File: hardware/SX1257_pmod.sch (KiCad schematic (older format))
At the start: 50 parts, among them J1 Conn_02x06_Odd_Even, J2 SMA_F_RX, J3 SMA_F_TX, U1 SX1257, U2 SC18IS602B, Y1 32/36MHz ?ppm

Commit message: PCB design almost done.
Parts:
- removed AE1, AE2: PCB_Ant, symbol Device:Antenna
- removed R3, R4, R5, R6: 0R, Resistor_SMD:R_0603_1608Metric, symbol Device:R
- J2, J3: footprint Connector_Coaxial:SMA_Amphenol_132134-10_Vertical -> extra:CON-SMA-EDGE
- Y1: value 32/36MHz ?ppm -> 36MHz 10ppm; footprint Crystal:Crystal_SMD_5032-4Pin_5.0x3.2mm -> Crystal:Crystal_SMD_3225-4Pin_3.2x2.5mm; MfrNo (none) -> ABM8-36.000MHZ-10-1-U-T; Mouser (none) -> 815-ABM8-36-10-1-U-T; MouserURL (none) -> https://www.mouser.se/ProductDetail/ABRACON/ABM8-36000MHZ-1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
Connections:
- wire segments 186 -> 176
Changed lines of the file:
@@
 P 7450 4500
 F 0 "Y1" H 7500 4700 50  0000 L CNN
-F 1 "32/36MHz ?ppm" H 7500 4800 50  0000 L CNN
-F 2 "Crystal:Crystal_SMD_5032-4Pin_5.0x3.2mm" H 7450 4500 50  0001 C CNN
-F 3 "~" H 7450 4500 50  0001 C CNN
+F 1 "36MHz 10ppm" H 7500 4800 50  0000 L CNN
+F 2 "Crystal:Crystal_SMD_3225-4Pin_3.2x2.5mm" H 7450 4500 50  0001 C CNN
+F 3 "https://www.mouser.se/datasheet/2/3/abm8-16794.pdf" H 7450 4500 50  0001 C CNN
+F 4 "815-ABM8-36-10-1-U-T" H 7450 4500 50  0001 C CNN "Mouser"
+F 5 "https://www.mouser.se/ProductDetail/ABRACON/ABM8-36000MHZ-10-1-U-T?qs=sGAEpiMZZMsBj6bBr9Q9acVJ3l36SOAPXI0xqgGUahk%3d" H 7450 4500 50  0001 C CNN "MouserURL"
+F 6 "ABM8-36.000MHZ-10-1-U-T" H 7450 4500 50  0001 C CNN "MfrNo"
 	1    7450 4500
 	1    0    0    -1
@@
 F 0 "J3" H 4499 5276 50  0000 L CNN
 F 1 "SMA_F_TX" H 4499 5185 50  0000 L CNN
-F 2 "Connector_Coaxial:SMA_Amphenol_132134-10_Vertical" H 4400 5300 50  0001 C CNN
+F 2 "extra:CON-SMA-EDGE" H 4400 5300 50  0001 C CNN
 F 3 " ~" H 4400 5300 50  0001 C CNN
 	1    4400 5300
@@
 Wire Wire Line
 	1450 6200 1450 6100
-Wire Wire Line
-	3450 5300 3550 5300
 $Comp
 L Device:C C5
@@
 Registers are available\nthrough SPI.
 $Comp
-L Device:Antenna AE2
-U 1 1 5C4B8B38
-P 4400 5100
-F 0 "AE2" V 4354 5230 50  0000 L CNN
-F 1 "PCB_Ant" V 4445 5230 50  0000 L CNN
-F 2 "" H 4400 5100 50  0001 C CNN
-F 3 "~" H 4400 5100 50  0001 C CNN
-	1    4400 5100
-	0    1    1    0
-$EndComp
-$Comp
-L Device:R R6
-U 1 1 5C4C50F2
-P 3850 5300
-F 0 "R6" V 3900 5450 50  0000 C CNN
-F 1 "0R" V 3850 5300 50  0000 C CNN
-F 2 "Resistor_SMD:R_0603_1608Metric" V 3780 5300 50  0001 C CNN
-F 3 "~" H 3850 5300 50  0001 C CNN
-	1    3850 5300
-	0    1    1    0
-$EndComp
-$Comp
-L Device:R R5
-U 1 1 5C4D0A85
-P 3850 5100
-F 0 "R5" V 3900 5250 50  0000 C CNN
-F 1 "0R" V 3850 5100 50  0000 C CNN
-F 2 "Resistor_SMD:R_0603_1608Metric" V 3780 5100 50  0001 C CNN
-F 3 "~" H 3850 5100 50  0001 C CNN
-	1    3850 5100
-	0    1    1    0
-$EndComp
-Wire Wire Line
-	3700 5100 3550 5100
-Wire Wire Line
-	3550 5100 3550 5300
-Connection ~ 3550 5300
-Wire Wire Line
-	3550 5300 3700 5300
-Wire Wire Line
-	4000 5100 4200 5100
-Wire Wire Line
-	4000 5300 4200 5300
-$Comp
 L Connector:Conn_Coaxial J2
 U 1 1 5C4EEF69
@@
 F 0 "J2" H 4499 3926 50  0000 L CNN
 F 1 "SMA_F_RX" H 4499 3835 50  0000 L CNN
-F 2 "Connector_Coaxial:SMA_Amphenol_132134-10_Vertical" H 4400 3950 50  0001 C CNN
+F 2 "extra:CON-SMA-EDGE" H 4400 3950 50  0001 C CNN
 F 3 " ~" H 4400 3950 50  0001 C CNN
 	1    4400 3950
@@
 Wire Wire Line
 	4400 4450 4400 4150
-$Comp
-L Device:Antenna AE1
-U 1 1 5C4EEF78
-P 4400 3750
-F 0 "AE1" V 4354 3880 50  0000 L CNN
-F 1 "PCB_Ant" V 4445 3880 50  0000 L CNN
-F 2 "" H 4400 3750 50  0001 C CNN
-F 3 "~" H 4400 3750 50  0001 C CNN
-	1    4400 3750
-	0    1    1    0
-$EndComp
-$Comp
-L Device:R R4
-U 1 1 5C4EEF7F
-P 3850 3950
-F 0 "R4" V 3900 4100 50  0000 C CNN
-F 1 "0R" V 3850 3950 50  0000 C CNN
-F 2 "Resistor_SMD:R_0603_1608Metric" V 3780 3950 50  0001 C CNN
-F 3 "~" H 3850 3950 50  0001 C CNN
-	1    3850 3950
-	0    1    1    0
-$EndComp
-$Comp
-L Device:R R3
-U 1 1 5C4EEF86
-P 3850 3750
-F 0 "R3" V 3900 3900 50  0000 C CNN
-F 1 "0R" V 3850 3750 50  0000 C CNN
-F 2 "Resistor_SMD:R_0603_1608Metric" V 3780 3750 50  0001 C CNN
-F 3 "~" H 3850 3750 50  0001 C CNN
-	1    3850 3750
-	0    1    1    0
-$EndComp
-Wire Wire Line
-	3700 3750 3550 3750
-Wire Wire Line
-	3550 3750 3550 3950
-Wire Wire Line
-	3550 3950 3700 3950
-Wire Wire Line
-	4000 3750 4200 3750
-Wire Wire Line
-	4000 3950 4200 3950
-Wire Wire Line
-	3550 3950 3250 3950
-Connection ~ 3550 3950
 Connection ~ 3250 3950
 Text Label 1000 1150 2    50   ~ 0
@@
 Wire Wire Line
 	13050 1500 13250 1500
+Wire Wire Line
+	3250 3950 4200 3950
+Wire Wire Line
+	3450 5300 4200 5300
 $EndSCHEMATC

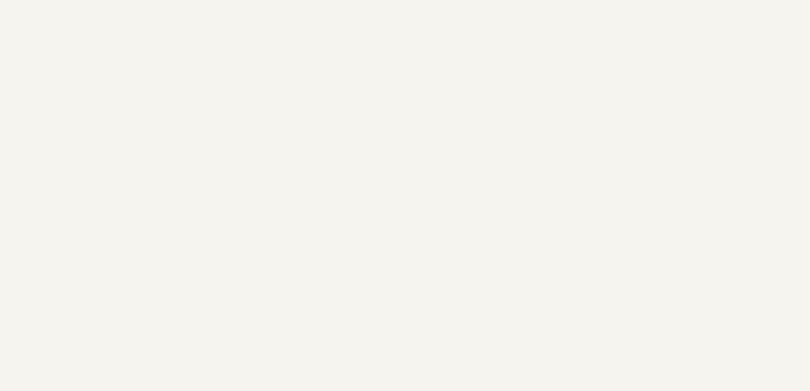
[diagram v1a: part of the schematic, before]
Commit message: RevA: Minor changes and produce gerbers
- Moved the SMA connectors closed to the edges
- Added silk on the back
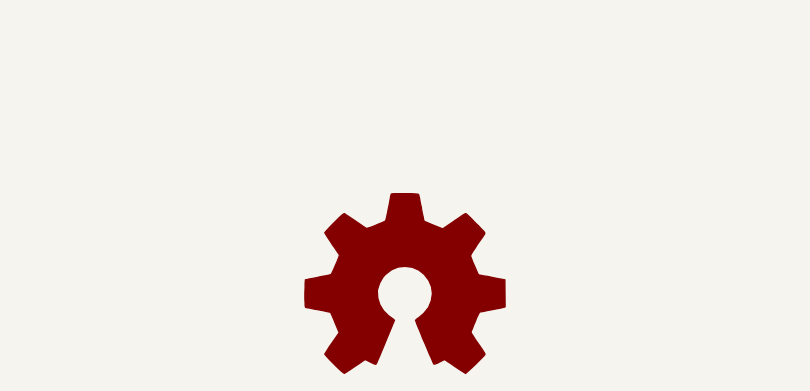
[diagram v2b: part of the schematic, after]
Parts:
- added LOGO1: Logo_Open_Hardware_Large, extra:oshw_logo, symbol Graphic:Logo_Open_Hardware_Large
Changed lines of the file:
@@
 Sheet 1 1
 Title "SX1257 PMOD"
-Date "2019-01-04"
+Date "2019-01-06"
 Rev "1.0"
 Comp ""
@@
 Wire Wire Line
 	3450 5300 4200 5300
+$Comp
+L Graphic:Logo_Open_Hardware_Large LOGO1
+U 1 1 5C32CA22
+P 11250 10600
+F 0 "LOGO1" H 11250 11100 50  0001 C CNN
+F 1 "Logo_Open_Hardware_Large" H 11250 10200 50  0001 C CNN
+F 2 "extra:oshw_logo" H 11250 10600 50  0001 C CNN
+F 3 "~" H 11250 10600 50  0001 C CNN
+	1    11250 10600
+	1    0    0    -1
+$EndComp
 $EndSCHEMATC

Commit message: Add souring info about SMA connector
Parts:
- J2, J3: LCSC (none) -> https://lcsc.com/product-detail/_RFsister-ANKX01-0093_C1296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; MfrNo (none) -> EMPCB.SMAFSTJ.B.HT; Mouser (none) -> 960-EMPCB.SMAFSTJBHT
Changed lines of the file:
@@
 	1450 4450 1450 4350
-$Comp
-L Connector:Conn_Coaxial J3
-U 1 1 5C3F0EA9
-P 4400 5300
-F 0 "J3" H 4499 5276 50  0000 L CNN
-F 1 "SMA_F_TX" H 4499 5185 50  0000 L CNN
-F 2 "extra:CON-SMA-EDGE" H 4400 5300 50  0001 C CNN
-F 3 " ~" H 4400 5300 50  0001 C CNN
-	1    4400 5300
-	1    0    0    -1
-$EndComp
 $Comp
 L power:GND #PWR011
@@
 F 1 "SMA_F_RX" H 4499 3835 50  0000 L CNN
 F 2 "extra:CON-SMA-EDGE" H 4400 3950 50  0001 C CNN
-F 3 " ~" H 4400 3950 50  0001 C CNN
+F 3 "https://eu.mouser.com/datasheet/2/398/EMPCB.SMAFSTJ.B.HT-19975.pdf" H 4400 3950 50  0001 C CNN
+F 4 "960-EMPCB.SMAFSTJBHT" H 4400 3950 50  0001 C CNN "Mouser"
+F 5 "EMPCB.SMAFSTJ.B.HT" H 4400 3950 50  0001 C CNN "MfrNo"
+F 6 "https://lcsc.com/product-detail/_RFsister-ANKX01-0093_C129604.html" H 4400 3950 50  0001 C CNN "LCSC"
 	1    4400 3950
 	1    0    0    -1
@@
 	1    0    0    -1
 $EndComp
+$Comp
+L Connector:Conn_Coaxial J3
+U 1 1 5C3ECE8D
+P 4400 5300
+F 0 "J3" H 4499 5276 50  0000 L CNN
+F 1 "SMA_F_TX" H 4499 5185 50  0000 L CNN
+F 2 "extra:CON-SMA-EDGE" H 4400 5300 50  0001 C CNN
+F 3 "https://eu.mouser.com/datasheet/2/398/EMPCB.SMAFSTJ.B.HT-19975.pdf" H 4400 5300 50  0001 C CNN
+F 4 "960-EMPCB.SMAFSTJBHT" H 4400 5300 50  0001 C CNN "Mouser"
+F 5 "EMPCB.SMAFSTJ.B.HT" H 4400 5300 50  0001 C CNN "MfrNo"
+F 6 "https://lcsc.com/product-detail/_RFsister-ANKX01-0093_C129604.html" H 4400 5300 50  0001 C CNN "LCSC"
+	1    4400 5300
+	1    0    0    -1
+$EndComp

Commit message: Swap pmod rows and add pull-ups.
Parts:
- added R1, R2: 2k2, Resistor_SMD:R_0603_1608Metric, symbol Device:R
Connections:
- net +3V3: now also R1.1, R2.1
- net CLK_IN: now also J1.8 (Pin_8); no longer J1.7 (Pin_7)
- net CLK_OUT: now also J1.6 (Pin_6); no longer J1.5 (Pin_5)
- net I2C_SDA: now also J1.10 (Pin_10), R2.2; no longer J1.9 (Pin_9)
- net I2C_CLK renamed I2C_SCL
- net I2C_SCL: now also J1.12 (Pin_12), R1.2; no longer J1.11 (Pin_11)
- net PMOD_5 renamed I_IN
- net I_IN: now also J1.11 (Pin_11); no longer J1.12 (Pin_12)
- net PMOD_6 renamed PMOD_2
- net PMOD_2: now also J1.9 (Pin_9); no longer J1.10 (Pin_10)
- net PMOD_7 renamed PMOD_3
- net PMOD_3: now also J1.7 (Pin_7); no longer J1.8 (Pin_8)
- net PMOD_8 renamed I_OUT
- net I_OUT: now also J1.5 (Pin_5); no longer J1.6 (Pin_6)
- no-connect marks 0 -> 1
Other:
- note added: "Icebreaker compatibility:\nPMOD_8 connects to P1A10 which is a global/clock input pin (IOB_3B_G6)"
- note removed: "Icebreaker compatibility:\nPMOD_4 connects to P1A10 which is a global/clock input pin (IOB_3B_G6)"
- moved on the sheet: FB1
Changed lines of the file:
@@
 Text Label 1000 2050 2    50   ~ 0
 PMOD_3
-Text Label 6550 2400 2    50   ~ 0
-PMOD_5
 Wire Wire Line
 	6750 2400 6550 2400
-Text Label 6550 2500 2    50   ~ 0
-PMOD_6
 Wire Wire Line
 	6750 2500 6550 2500
-Text Label 6550 2700 2    50   ~ 0
-PMOD_7
 Wire Wire Line
 	6750 2700 6550 2700
-Text Label 6550 2800 2    50   ~ 0
-PMOD_8
 Wire Wire Line
 	6750 2800 6550 2800
@@
 Text Label 1000 2150 2    50   ~ 0
 PMOD_4
-Text Label 1900 2050 0    50   ~ 0
+Text Label 1900 2550 0    50   ~ 0
 CLK_IN
 Wire Wire Line
@@
 Wire Wire Line
 	1000 1050 1200 1050
-Text Label 1000 2550 2    50   ~ 0
+Text Label 1000 3150 2    50   ~ 0
 PMOD_3V3
 $Comp
 L Device:Ferrite_Bead FB1
 U 1 1 5C30A1D4
-P 1450 2550
-F 0 "FB1" V 1550 2650 50  0000 C CNN
-F 1 "Ferrite_Bead" V 1250 2500 50  0001 C CNN
-F 2 "Inductor_SMD:L_0603_1608Metric" V 1380 2550 50  0001 C CNN
-F 3 "~" H 1450 2550 50  0001 C CNN
-	1    1450 2550
+P 1450 3150
+F 0 "FB1" V 1550 3250 50  0000 C CNN
+F 1 "Ferrite_Bead" V 1250 3100 50  0001 C CNN
+F 2 "Inductor_SMD:L_0603_1608Metric" V 1380 3150 50  0001 C CNN
+F 3 "~" H 1450 3150 50  0001 C CNN
+	1    1450 3150
 	0    1    1    0
 $EndComp
 Wire Wire Line
-	1000 2550 1300 2550
+	1000 3150 1300 3150
 $Comp
 L power:+3V3 #PWR03
 U 1 1 5C30B964
-P 2050 2500
-F 0 "#PWR03" H 2050 2350 50  0001 C CNN
-F 1 "+3V3" H 1950 2650 50  0000 L CNN
-F 2 "" H 2050 2500 50  0001 C CNN
-F 3 "" H 2050 2500 50  0001 C CNN
-	1    2050 2500
+P 2050 3100
+F 0 "#PWR03" H 2050 2950 50  0001 C CNN
+F 1 "+3V3" H 1950 3250 50  0000 L CNN
+F 2 "" H 2050 3100 50  0001 C CNN
+F 3 "" H 2050 3100 50  0001 C CNN
+	1    2050 3100
 	-1   0    0    -1
 $EndComp
@@
 L power:PWR_FLAG #FLG01
 U 1 1 5C3103FC
-P 1900 2500
-F 0 "#FLG01" H 1900 2575 50  0001 C CNN
-F 1 "PWR_FLAG" H 1900 2674 50  0001 C CNN
-F 2 "" H 1900 2500 50  0001 C CNN
-F 3 "~" H 1900 2500 50  0001 C CNN
-	1    1900 2500
-	1    0    0    -1
-$EndComp
-Wire Wire Line
-	1900 2500 1900 2550
-Connection ~ 1900 2550
-Wire Wire Line
-	2050 2550 2050 2500
-Wire Wire Line
-	1900 2550 2050 2550
+P 1900 3100
+F 0 "#FLG01" H 1900 3175 50  0001 C CNN
+F 1 "PWR_FLAG" H 1900 3274 50  0001 C CNN
+F 2 "" H 1900 3100 50  0001 C CNN
+F 3 "~" H 1900 3100 50  0001 C CNN
+	1    1900 3100
+	1    0    0    -1
+$EndComp
+Wire Wire Line
+	1900 3100 1900 3150
+Connection ~ 1900 3150
+Wire Wire Line
+	2050 3150 2050 3100
+Wire Wire Line
+	1900 3150 2050 3150
 Text Label 8850 2100 0    50   ~ 0
 DIO0
@@
 L power:PWR_FLAG #FLG02
 U 1 1 5C3953E6
-P 1900 2850
-F 0 "#FLG02" H 1900 2925 50  0001 C CNN
-F 1 "PWR_FLAG" H 1900 3024 50  0001 C CNN
-F 2 "" H 1900 2850 50  0001 C CNN
-F 3 "~" H 1900 2850 50  0001 C CNN
-	1    1900 2850
+P 1900 3450
+F 0 "#FLG02" H 1900 3525 50  0001 C CNN
+F 1 "PWR_FLAG" H 1900 3624 50  0001 C CNN
+F 2 "" H 1900 3450 50  0001 C CNN
+F 3 "~" H 1900 3450 50  0001 C CNN
+	1    1900 3450
 	-1   0    0    1
 $EndComp
@@
 Wire Wire Line
 	1700 1150 1900 1150
-Text Label 1000 2750 2    50   ~ 0
+Text Label 1000 3350 2    50   ~ 0
 PMOD_GND
 $Comp
 L power:GND #PWR04
 U 1 1 5C3092FD
-P 2050 2850
-F 0 "#PWR04" H 2050 2600 50  0001 C CNN
-F 1 "GND" H 2055 2677 50  0000 C CNN
-F 2 "" H 2050 2850 50  0001 C CNN
-F 3 "" H 2050 2850 50  0001 C CNN
-	1    2050 2850
-	1    0    0    -1
-$EndComp
-Wire Wire Line
-	2050 2750 2050 2850
-Wire Wire Line
-	1900 2850 1900 2750
-Connection ~ 1900 2750
-Wire Wire Line
-	1900 2750 2050 2750
+P 2050 3450
+F 0 "#PWR04" H 2050 3200 50  0001 C CNN
+F 1 "GND" H 2055 3277 50  0000 C CNN
+F 2 "" H 2050 3450 50  0001 C CNN
+F 3 "" H 2050 3450 50  0001 C CNN
+	1    2050 3450
+	1    0    0    -1
+$EndComp
+Wire Wire Line
+	2050 3350 2050 3450
+Wire Wire Line
+	1900 3450 1900 3350
+Connection ~ 1900 3350
+Wire Wire Line
+	1900 3350 2050 3350
 Wire Wire Line
 	6550 1600 6750 1600
@@
 Text Label 13250 1500 0    50   ~ 0
 SPI_NSS
-Text Label 1900 2150 0    50   ~ 0
+Text Label 1900 2650 0    50   ~ 0
 CLK_OUT
-Text Label 1900 1850 0    50   ~ 0
-I2C_CLK
-Text Label 1900 1950 0    50   ~ 0
+Text Label 1900 2350 0    50   ~ 0
+I2C_SCL
+Text Label 1900 2450 0    50   ~ 0
 I2C_SDA
 $Comp
@@
 	11750 1900 11550 1900
 Text Label 11550 1800 2    50   ~ 0
-I2C_CLK
+I2C_SCL
 Text Label 11550 1700 2    50   ~ 0
 I2C_SDA
-Wire Wire Line
-	11550 1700 11750 1700
-Wire Wire Line
-	11550 1800 11750 1800
 $Comp
 L Device:R R9
@@
 I2C_INT
 Text Notes 550  700  0    50   ~ 0
-Icebreaker compatibility:\nPMOD_4 connects to P1A10 which is a global/clock input pin (IOB_3B_G6)
+Icebreaker compatibility:\nPMOD_8 connects to P1A10 which is a global/clock input pin (IOB_3B_G6)
 Text Label 3550 2350 0    50   ~ 0
 DIO0
@@
 	1000 2150 1900 2150
 Wire Wire Line
-	1600 2550 1900 2550
-Wire Wire Line
-	1000 2750 1900 2750
+	1600 3150 1900 3150
+Wire Wire Line
+	1000 3350 1900 3350
 Wire Wire Line
 	13050 1500 13250 1500
@@
 	1    0    0    -1
 $EndComp
+Text Label 1000 2350 2    50   ~ 0
+PMOD_5
+Text Label 1000 2450 2    50   ~ 0
+PMOD_6
+Text Label 1000 2550 2    50   ~ 0
+PMOD_7
+Text Label 1000 2650 2    50   ~ 0
+PMOD_8
+Wire Wire Line
+	1000 2350 1900 2350
+Wire Wire Line
+	1000 2450 1900 2450
+Wire Wire Line
+	1000 2550 1900 2550
+Wire Wire Line
+	1000 2650 1900 2650
+Text Label 1900 1850 0    50   ~ 0
+I_IN
+Text Label 1900 1950 0    50   ~ 0
+Q_IN
+Text Label 1900 2050 0    50   ~ 0
+Q_OUT
+Text Label 1900 2150 0    50   ~ 0
+I_OUT
+Text Label 6550 2400 2    50   ~ 0
+I_IN
+Text Label 6550 2500 2    50   ~ 0
+Q_IN
+Text Label 6550 2700 2    50   ~ 0
+Q_OUT
+Text Label 6550 2800 2    50   ~ 0
+I_OUT
+$Comp
+L Device:R R2
+U 1 1 5C809682
+P 11150 1250
+F 0 "R2" H 11220 1296 50  0000 L CNN
+F 1 "2k2" H 11220 1205 50  0000 L CNN
+F 2 "Resistor_SMD:R_0603_1608Metric" V 11080 1250 50  0001 C CNN
+F 3 "~" H 11150 1250 50  0001 C CNN
+	1    11150 1250
+	1    0    0    -1
+$EndComp
+$Comp
+L Device:R R1
+U 1 1 5C8096F4
+P 10850 1250
+F 0 "R1" H 10920 1296 50  0000 L CNN
+F 1 "2k2" H 10920 1205 50  0000 L CNN
+F 2 "Resistor_SMD:R_0603_1608Metric" V 10780 1250 50  0001 C CNN
+F 3 "~" H 10850 1250 50  0001 C CNN
+	1    10850 1250
+	1    0    0    -1
+$EndComp
+Wire Wire Line
+	11150 1400 11150 1700
+Wire Wire Line
+	11150 1700 11750 1700
+Wire Wire Line
+	10850 1800 10850 1400
+Wire Wire Line
+	10850 1800 11750 1800
+$Comp
+L power:+3V3 #PWR0101
+U 1 1 5C84AE58
+P 11150 1000
+F 0 "#PWR0101" H 11150 850 50  0001 C CNN
+F 1 "+3V3" H 11050 1150 50  0000 L CNN
+F 2 "" H 11150 1000 50  0001 C CNN
+F 3 "" H 11150 1000 50  0001 C CNN
+	1    11150 1000
+	-1   0    0    -1
+$EndComp
+Wire Wire Line
+	11150 1000 11150 1100
+$Comp
+L power:+3V3 #PWR0102
+U 1 1 5C854300
+P 10850 1000
+F 0 "#PWR0102" H 10850 850 50  0001 C CNN
+F 1 "+3V3" H 10750 1150 50  0000 L CNN
+F 2 "" H 10850 1000 50  0001 C CNN
+F 3 "" H 10850 1000 50  0001 C CNN
+	1    10850 1000
+	-1   0    0    -1
+$EndComp
+Wire Wire Line
+	10850 1000 10850 1100
+NoConn ~ 11550 1900
 $EndSCHEMATC

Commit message: RevB improvements
- Clean up routing and improve ground plane
- Change crystal to 1.6x1.2mm
- Minor improvements everywhere
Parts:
- Y1: footprint Crystal:Crystal_SMD_3225-4Pin_3.2x2.5mm -> extra:Crystal_SMD_1612-4Pin_1.6x1.2mm; MfrNo ABM8-36.000MHZ-10-1-U-T -> ABM12W-36.0000MHZ-6-B1U-T3; Mouser 815-ABM8-36-10-1-U-T -> 815-12W36-6B1UT; MouserURL https://www.mouser.se/ProductDetail/ABRACON/ABM8-36000MHZ-1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 -> https://eu.mouser.com/ProductDetail/ABRACON/ABM12W-360000MH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
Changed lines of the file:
@@
 EESchema Schematic File Version 4
 LIBS:SX1257_pmod-cache
-EELAYER 26 0
+EELAYER 29 0
 EELAYER END
 $Descr A3 16535 11693
@@
 Sheet 1 1
 Title "SX1257 PMOD"
-Date "2019-01-06"
-Rev "1.0"
+Date "2019-05-07"
+Rev "RevB"
 Comp ""
 Comment1 ""
@@
 F 0 "Y1" H 7500 4700 50  0000 L CNN
 F 1 "36MHz 10ppm" H 7500 4800 50  0000 L CNN
-F 2 "Crystal:Crystal_SMD_3225-4Pin_3.2x2.5mm" H 7450 4500 50  0001 C CNN
-F 3 "https://www.mouser.se/datasheet/2/3/abm8-16794.pdf" H 7450 4500 50  0001 C CNN
-F 4 "815-ABM8-36-10-1-U-T" H 7450 4500 50  0001 C CNN "Mouser"
-F 5 "https://www.mouser.se/ProductDetail/ABRACON/ABM8-36000MHZ-10-1-U-T?qs=sGAEpiMZZMsBj6bBr9Q9acVJ3l36SOAPXI0xqgGUahk%3d" H 7450 4500 50  0001 C CNN "MouserURL"
-F 6 "ABM8-36.000MHZ-10-1-U-T" H 7450 4500 50  0001 C CNN "MfrNo"
+F 2 "extra:Crystal_SMD_1612-4Pin_1.6x1.2mm" H 7450 4500 50  0001 C CNN
+F 3 "https://eu.mouser.com/datasheet/2/3/ABM12W-1107622.pdf" H 7450 4500 50  0001 C CNN
+F 4 "815-12W36-6B1UT" H 7450 4500 50  0001 C CNN "Mouser"
+F 5 "https://eu.mouser.com/ProductDetail/ABRACON/ABM12W-360000MHZ-6-B1U-T3?qs=%2Fha2pyFaduiSskzRnk5YszYp%2FYQbyNEaqk3XaFpHyq5uanwnbHUz6heQId99%2FXtKk4c7I0zJw7I%3D" H 7450 4500 50  0001 C CNN "MouserURL"
+F 6 "ABM12W-36.0000MHZ-6-B1U-T3" H 7450 4500 50  0001 C CNN "MfrNo"
 	1    7450 4500
 	1    0    0    -1

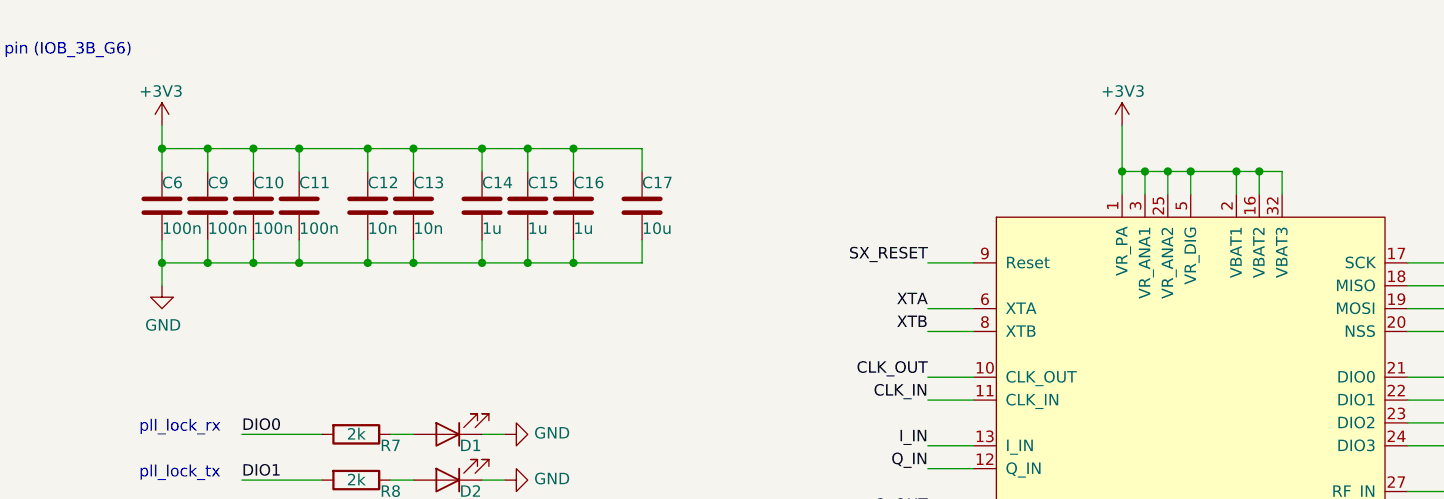
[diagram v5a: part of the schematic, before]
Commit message: Fix VR_* pins & change most passives to 0402
This fixes the power pin wiring as mentioned in the RevB errata:
SX1257 VR_* pins are now only connected to decoupling caps.

This also moves a lot of caps away from the PMOD header & closer to
the appropriate power pins.

Space was getting tight, so this also changes small caps & inductors
to 0402. As a result, there's also a bit of re-routing to reconnect things.
The RF paths should flow a bit better now.
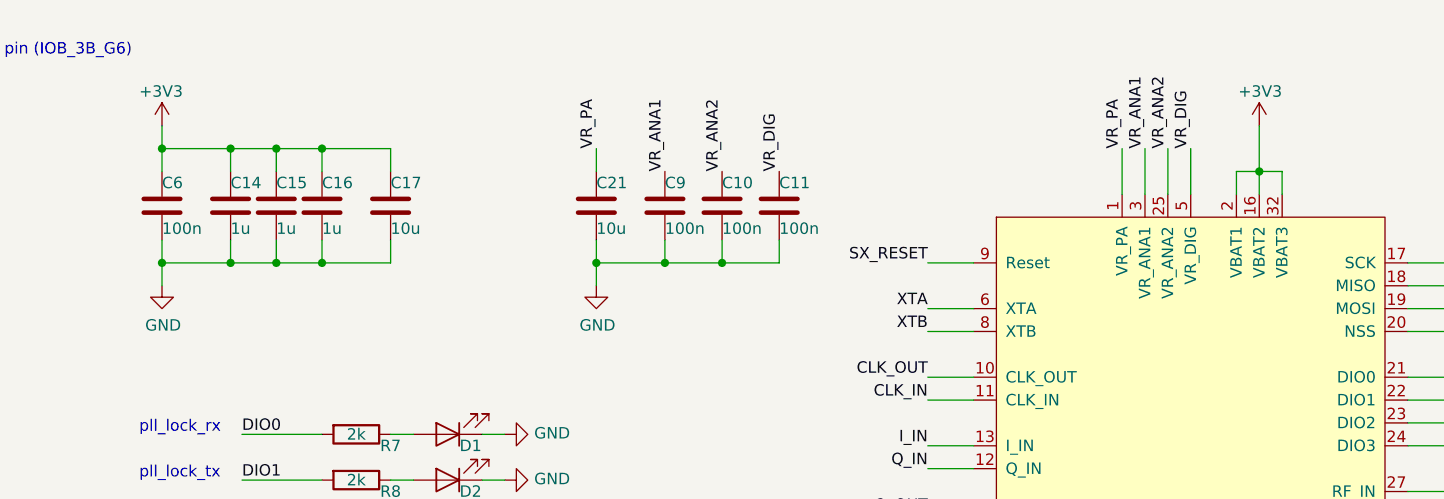
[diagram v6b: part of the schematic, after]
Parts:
- removed C12, C13: 10n, Capacitor_SMD:C_0603_1608Metric, symbol Device:C
- added C21: 10u, Capacitor_SMD:C_0603_1608Metric, symbol Device:C
- C1, C10, C11, C14, C15, C16, C18, C19, C2, C20, C3, C4, C5, C6, C7, C8, C9: footprint Capacitor_SMD:C_0603_1608Metric -> Capacitor_SMD:C_0402_1005Metric
- L1, L2, L3: footprint Inductor_SMD:L_0603_1608Metric -> Inductor_SMD:L_0402_1005Metric
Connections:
- net +3V3: no longer C10.1, C11.1, C9.1, U1.1 (VR_PA), U1.25 (VR_ANA2), U1.3 (VR_ANA1), U1.5 (VR_DIG)
- net GND: now also C21.2
- new net VR_ANA1: C9.1, U1.3 (VR_ANA1)
- new net VR_ANA2: C10.1, U1.25 (VR_ANA2)
- new net VR_DIG: C11.1, U1.5 (VR_DIG)
- new net VR_PA: C21.1, U1.1 (VR_PA)
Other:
- moved on the sheet: C10, C11, C14, C15, C16, C17, C9
